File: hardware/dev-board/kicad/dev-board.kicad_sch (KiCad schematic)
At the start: 0 parts

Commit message: Update Files
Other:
- sheet ICM-20608G renamed General Purpose IMU
- sheet KX134-1211 renamed High G Accelerometer
- sheet MS5611 renamed Barometer
- added sheet GPS (hierarchical_sheets/zoe-m8q.kicad_sch)
- added sheet Magnetometer (hierarchical_sheets/mmc5983ma.kicad_sch)

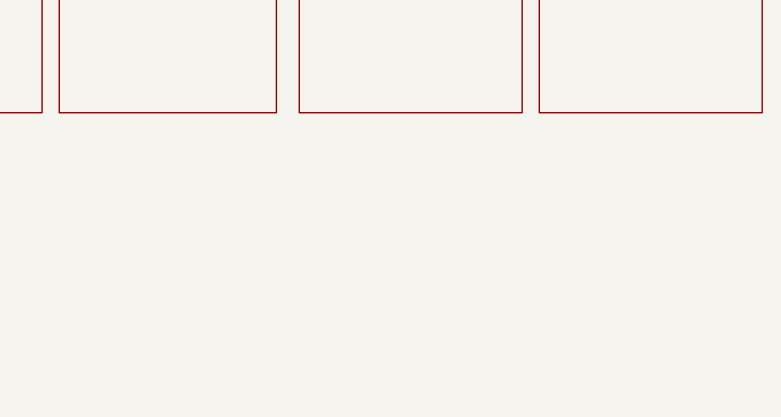
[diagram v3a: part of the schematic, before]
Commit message: finished GPSschematic
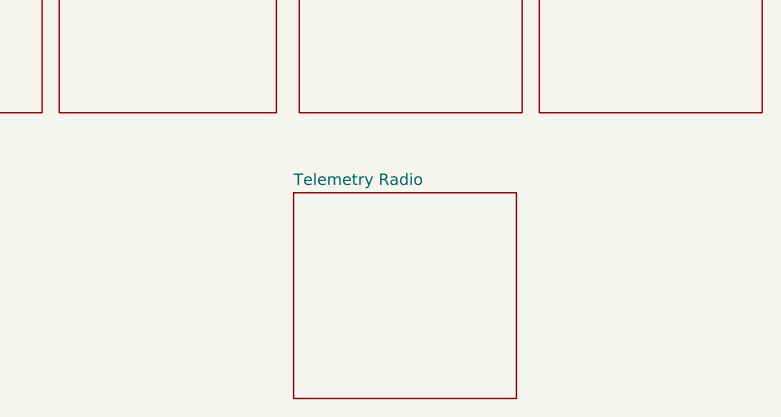
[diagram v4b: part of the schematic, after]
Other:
- added sheet Telemetry Radio (hierarchical_sheets/sx1262.kicad_sch)
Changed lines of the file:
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@@
+    )
+  )
+  (sheet (at 170.815 90.17) (size 24.765 22.86) (fields_autoplaced)
+    (stroke (width 0.1524) (type solid) (color 0 0 0 0))
+    (fill (color 255 255 194 1.0000))
+    (property "Sheet name" "Telemetry Radio" (id 0) (at 170.815 89.4584 0)
+      (effects (font (size 1.27 1.27)) (justify left bottom))
+    )
+    (property "Sheet file" "hierarchical_sheets/sx1262.kicad_sch" (id 1) (at 170.815 113.6146 0)
+      (effects (font (size 1.27 1.27)) (justify left top) hide)
     )
   )
@@
     (path "/4df84968-9e4f-499d-a301-87e9b49593a0" (page "6"))
     (path "/aac83767-0099-4d8a-bb8e-c64d3232847f" (page "7"))
+    (path "/602f4caf-b9d3-45bf-9e3b-788a618f0058" (page "8"))
   )
   (symbol_instances
@@
       (reference "#PWR?") (unit 1) (value "+3V3") (footprint "")
     )
-    (path "/aac83767-0099-4d8a-bb8e-c64d3232847f/fa135ae3-5704-436c-b3b8-0867a63a5ef3"
-      (reference "#PWR?") (unit 1) (value "GND") (footprint "")
-    )
     (path "/e5dd472d-0147-4d93-be86-6e3d2b752417/54a30f3f-ae95-42a2-b47b-42237bf566f3"
       (reference "C1") (unit 1) (value "10nF") (footprint "")
@@
       (reference "JP?") (unit 1) (value "SolderJumper_2_Open") (footprint "Jumper:SolderJumper-2_P1.3mm_Open_RoundedPad1.0x1.5mm")
     )
-    (path "/aac83767-0099-4d8a-bb8e-c64d3232847f/2b8e48c8-8702-4ac5-9b05-393e32fbad9d"
-      (reference "JP?") (unit 1) (value "SolderJumper_2_Open") (footprint "Jumper:SolderJumper-2_P1.3mm_Open_RoundedPad1.0x1.5mm")
-    )
     (path "/aac83767-0099-4d8a-bb8e-c64d3232847f/67b8ac51-465d-4daa-92e0-75034918ccaa"
       (reference "JP?") (unit 1) (value "SolderJumper_2_Open") (footprint "Jumper:SolderJumper-2_P1.3mm_Open_RoundedPad1.0x1.5mm")
     )
+    (path "/aac83767-0099-4d8a-bb8e-c64d3232847f/6f81843e-c373-4d63-b50b-6b3c15e4ba2d"
+      (reference "JP?") (unit 1) (value "SolderJumper_2_Open") (footprint "Jumper:SolderJumper-2_P1.3mm_Open_RoundedPad1.0x1.5mm")
+    )
     (path "/aac83767-0099-4d8a-bb8e-c64d3232847f/783df045-e783-48bc-93b2-9b16531a8d9b"
       (reference "JP?") (unit 1) (value "SolderJumper_2_Open") (footprint "Jumper:SolderJumper-2_P1.3mm_Open_RoundedPad1.0x1.5mm")
     )
     (path "/aac83767-0099-4d8a-bb8e-c64d3232847f/79086c16-ae67-4efb-b5de-4e5e958ee902"
+      (reference "JP?") (unit 1) (value "SolderJumper_2_Open") (footprint "Jumper:SolderJumper-2_P1.3mm_Open_RoundedPad1.0x1.5mm")
+    )
+    (path "/aac83767-0099-4d8a-bb8e-c64d3232847f/961ed7ae-6761-42cd-865f-d264883f31ce"
+      (reference "JP?") (unit 1) (value "SolderJumper_3_Open") (footprint "Jumper:SolderJumper-3_P1.3mm_Bridged12_RoundedPad1.0x1.5mm")
+    )
+    (path "/aac83767-0099-4d8a-bb8e-c64d3232847f/fb87cf30-3827-4eb5-af03-f09f9967b4c7"
       (reference "JP?") (unit 1) (value "SolderJumper_2_Open") (footprint "Jumper:SolderJumper-2_P1.3mm_Open_RoundedPad1.0x1.5mm")
     )
@@
       (reference "R4") (unit 1) (value "47Ω") (footprint "")
     )
-    (path "/aac83767-0099-4d8a-bb8e-c64d3232847f/3c082c03-b2b9-4bee-a501-92787a268a6a"
-      (reference "R?") (unit 1) (value "10K") (footprint "")
-    )
-    (path "/aac83767-0099-4d8a-bb8e-c64d3232847f/4b52e462-b9a5-434a-aa4b-ab1ee9566aef"
-      (reference "R?") (unit 1) (value "10K") (footprint "")
-    )
     (path "/e5dd472d-0147-4d93-be86-6e3d2b752417/fcdb7807-0bfa-4cc7-8f22-9b403312714d"
       (reference "TP1") (unit 1) (value "Header") (footprint "Connector_PinHeader_2.54mm:PinHeader_1x01_P2.54mm_Vertical")
@@
       (reference "TP?") (unit 1) (value "Header") (footprint "Connector_PinHeader_2.54mm:PinHeader_1x01_P2.54mm_Vertical")
     )
+    (path "/aac83767-0099-4d8a-bb8e-c64d3232847f/2f643400-5a36-4bdf-82af-29fe092842fe"
+      (reference "TP?") (unit 1) (value "Header") (footprint "Connector_PinHeader_2.54mm:PinHeader_1x01_P2.54mm_Vertical")
+    )
+    (path "/aac83767-0099-4d8a-bb8e-c64d3232847f/31bd57f0-7747-49a5-9e72-b472ea09de2a"
+      (reference "TP?") (unit 1) (value "Header") (footprint "Connector_PinHeader_2.54mm:PinHeader_1x01_P2.54mm_Vertical")
+    )
     (path "/aac83767-0099-4d8a-bb8e-c64d3232847f/5def7c4b-ab28-4048-857b-6075bf53ffed"
       (reference "TP?") (unit 1) (value "Header") (footprint "Connector_PinHeader_2.54mm:PinHeader_1x01_P2.54mm_Vertical")
@@
       (reference "TP?") (unit 1) (value "Header") (footprint "Connector_PinHeader_2.54mm:PinHeader_1x01_P2.54mm_Vertical")
     )
-    (path "/aac83767-0099-4d8a-bb8e-c64d3232847f/8c218e47-f7cc-4340-b28a-44ad16e0094d"
+    (path "/aac83767-0099-4d8a-bb8e-c64d3232847f/8b8dccf4-24fd-4d63-9e75-9aea5fb0e203"
       (reference "TP?") (unit 1) (value "Header") (footprint "Connector_PinHeader_2.54mm:PinHeader_1x01_P2.54mm_Vertical")
     )
@@
       (reference "TP?") (unit 1) (value "Header") (footprint "Connector_PinHeader_2.54mm:PinHeader_1x01_P2.54mm_Vertical")
     )
+    (path "/aac83767-0099-4d8a-bb8e-c64d3232847f/de77de17-d39a-42a7-86f6-72c4b920738f"
+      (reference "TP?") (unit 1) (value "Header") (footprint "Connector_PinHeader_2.54mm:PinHeader_1x01_P2.54mm_Vertical")
+    )
